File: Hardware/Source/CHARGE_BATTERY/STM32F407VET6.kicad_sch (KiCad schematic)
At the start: 3 parts, among them U2 STM32F407VET6, Y1 Crystal_8MHz_SMD-4PIN

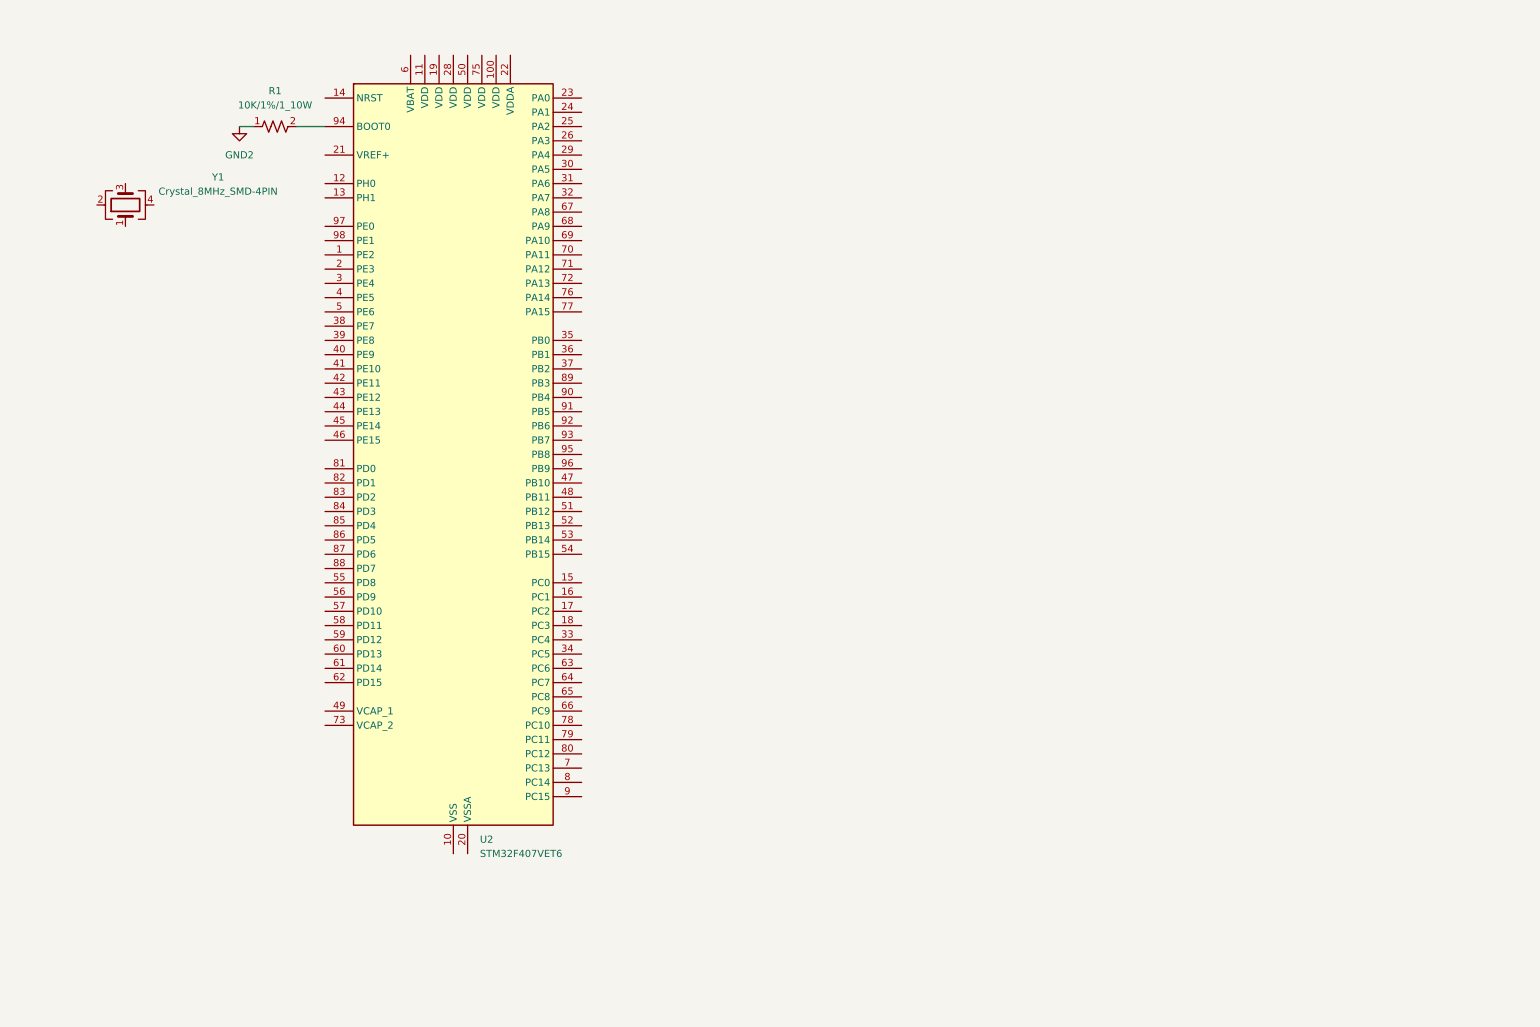
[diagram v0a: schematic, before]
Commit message: Combine Sche in Source: PFC, LLC, F1, F4, ESP32
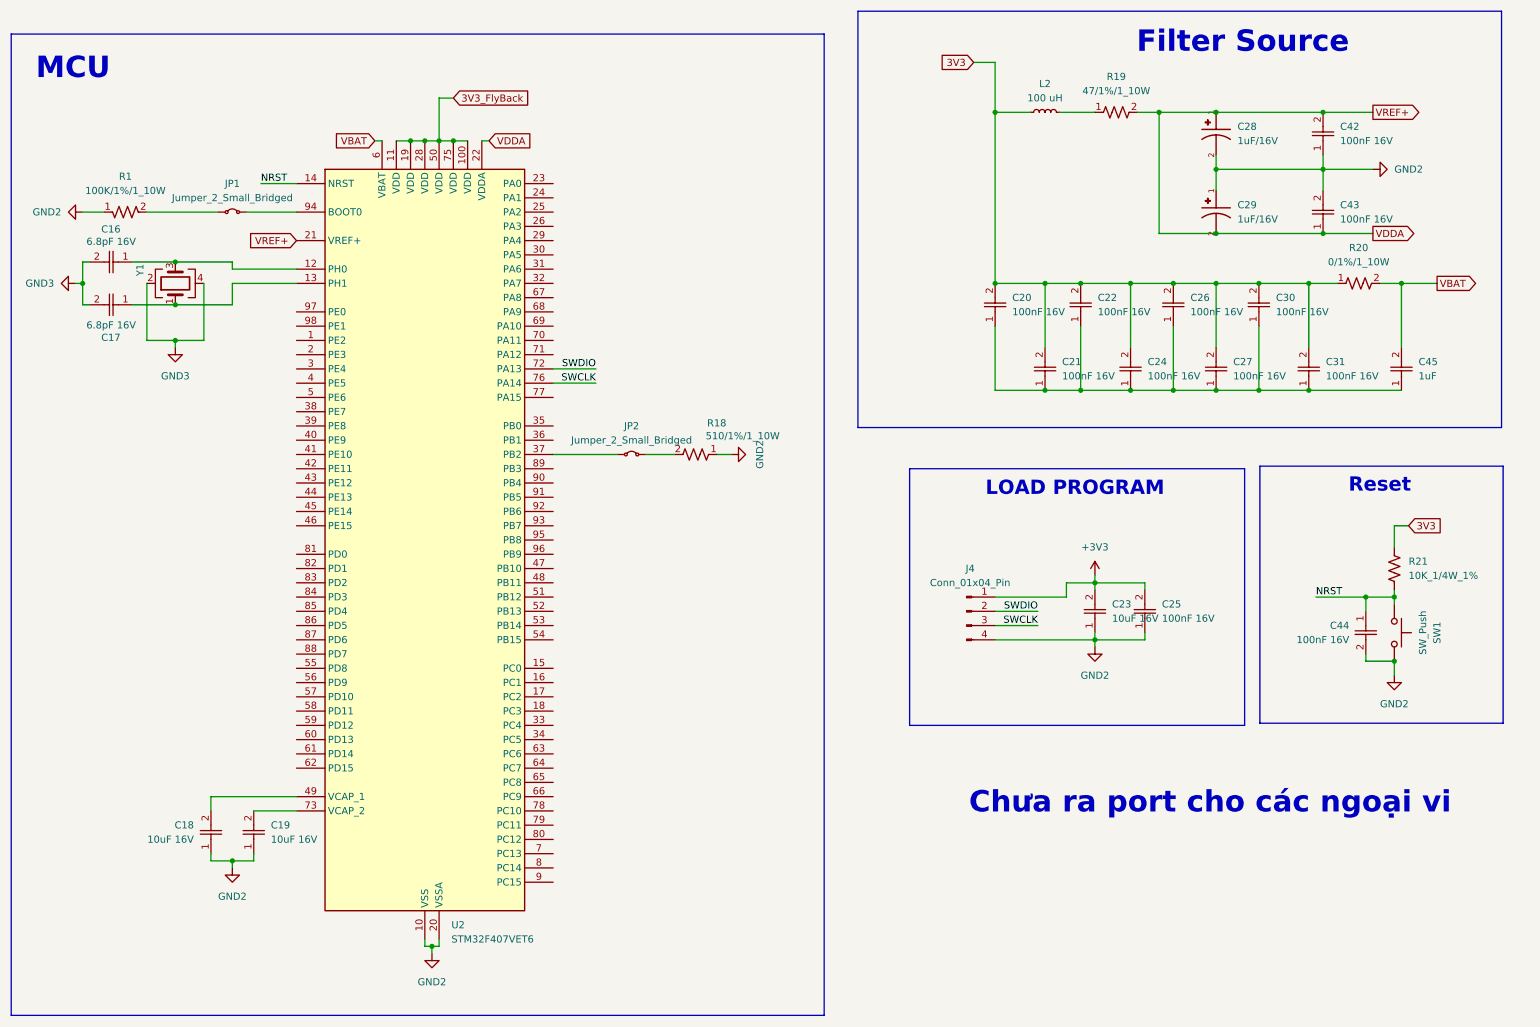
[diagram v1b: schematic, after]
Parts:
- removed R1: 10K/1%/1_10W, charge_battery_footprint_lib:Res_10K_0603, symbol charge_battery_sym_lib:Res_10K_0603_1%
- added C16, C17: 6.8pF 16V, charge_battery_footprint_lib:C_0603_1608Metric, symbol charge_battery_sym_lib:Ceramic_Cap_SMD_100nF_16V
- added C18, C19, C23: 10uF 16V, charge_battery_footprint_lib:Ceramic_Cap_10uF_16V, symbol charge_battery_sym_lib:Ceramic_Cap_SMD_10uF_16V
- added C20, C21, C22, C24, C25, C26, C27, C30, C31, C42, C43, C44: 100nF 16V, charge_battery_footprint_lib:C_0603_1608Metric, symbol charge_battery_sym_lib:Ceramic_Cap_SMD_100nF_16V
- added C28, C29: 1uF/16V, charge_battery_footprint_lib:Cap_Tantalum_1uF_16V, symbol charge_battery_sym_lib:Cap_Tantalum_1uF_16V
- added C45: 1uF, charge_battery_footprint_lib:Ceramic_Cap_Hole_1uF_50V, symbol charge_battery_sym_lib:Ceramic_Cap_Hole_1uF_50V_
- added J4: Conn_01x04_Pin, symbol Connector:Conn_01x04_Pin
- added JP1, JP2: Jumper_2_Small_Bridged, TestPoint:TestPoint_2Pads_Pitch2.54mm_Drill0.8mm, symbol Jumper:Jumper_2_Small_Bridged
- added L2: 100 uH, symbol Device:L_Small
- added R1: 100K/1%/1_10W, charge_battery_footprint_lib:Res_200K_0603, symbol charge_battery_sym_lib:Res_200K_0603_1%
- added R18: 510/1%/1_10W, charge_battery_footprint_lib:Res_10K_0603, symbol charge_battery_sym_lib:Res_10K_0603_1%
- added R19: 47/1%/1_10W, charge_battery_footprint_lib:Res_10K_0603, symbol charge_battery_sym_lib:Res_10K_0603_1%
- added R20: 0/1%/1_10W, charge_battery_footprint_lib:Res_10K_0603, symbol charge_battery_sym_lib:Res_10K_0603_1%
- added R21: 10K_1/4W_1%, charge_battery_footprint_lib:Res_10K_1_4W_1%, symbol charge_battery_sym_lib:Res_hole_10K_1/4W_1%
- added SW1: SW_Push, charge_battery_footprint_lib:SW_SMD, symbol charge_battery_sym_lib:SW_Push
- Y1: footprint charge_battery_footprint_lib:Crystal_8MHz_SMD-4PIN -> charge_battery_footprint_lib:IPP65R095C7
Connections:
- net GND2: now also U2.10 (VSS), U2.20 (VSSA), U2.27 (VSS), U2.74 (VSS), U2.99 (VSS), C18.1, C19.1, C23.1, C25.1, C28.2, C29.1, C42.1, C43.2, C44.2, J4.4 (Pin_4), R1.1, R18.1, SW1.1
- net at Y1.1: now also U2.13 (PH1), C17.1
- net GND3: now reaches Y1.2
- net GND3: now also Y1.4, C16.2, C17.2
- net at Y1.3: now also U2.12 (PH0), C16.1
- net at U2.94 (BOOT0): now also JP1.2 (B)
- net 3V3_FlyBack: now reaches U2.100 (VDD)
- net 3V3_FlyBack: now also U2.11 (VDD), U2.19 (VDD), U2.28 (VDD), U2.50 (VDD), U2.75 (VDD)
- net NRST: now reaches U2.14 (NRST)
- net NRST: now also C44.1, R21.1, SW1.2
- net VDDA: now reaches U2.21 (VREF+)
- net VDDA: now also U2.22 (VDDA), C28.1, C29.2, C42.2, C43.1, R19.2
- net at U2.37 (PB2): now also JP2.1 (A)
- net at U2.49 (VCAP_1): now also C18.2
- net VBAT: now reaches U2.6 (VBAT)
- net VBAT: now also C45.2, R20.2
- net SWDIO: now reaches U2.72 (PA13)
- net SWDIO: now also J4.2 (Pin_2)
- net at U2.73 (VCAP_2): now also C19.2
- net SWCLK: now reaches U2.76 (PA14)
- net SWCLK: now also J4.3 (Pin_3)
- new net: C20.1, C21.1, C22.1, C24.1, C26.1, C27.1, C30.1, C31.1, C45.1
- new net: JP1.1 (A), R1.2
- new net: L2.2, R19.1
- new net: JP2.2 (B), R18.2
- new net +3V3: C23.2, C25.2, J4.1 (Pin_1)
- new net 3V3: C20.2, C21.2, C22.2, C24.2, C26.2, C27.2, C30.2, C31.2, L2.1, R20.1, R21.2
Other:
- note added: "Chưa ra port cho các ngoại vi"
- note added: "Filter Source"
- note added: "LOAD PROGRAM"
- note added: "MCU"
- note added: "Reset"

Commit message: Merge branch 'dev_hardware' of https://github.com/DONGKHOA/CHARGE_BATTERY into dev_hardware
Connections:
- net 3V3 is gone; now on net +3V3: C20.2, C21.2, C22.2, C24.2, C26.2, C27.2, C30.2, C31.2, L2.1, R20.1, R21.2
- net 3V3_FlyBack is gone; now on net +3V3: U2.100 (VDD), U2.11 (VDD), U2.19 (VDD), U2.28 (VDD), U2.50 (VDD), U2.75 (VDD)
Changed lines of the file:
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@@
-	(wire
-		(pts
-			(xy 186.69 24.13) (xy 190.5 24.13)
-		)
-		(stroke
-			(width 0)
-			(type default)
-		)
-	)
 	(wire
 		(pts
@@
 	(wire
 		(pts
-			(xy 93.98 30.48) (xy 91.44 30.48)
-		)
-		(stroke
-			(width 0)
-			(type default)
-		)
-	)
-	(wire
-		(pts
 			(xy 59.69 45.72) (xy 66.04 45.72)
 		)
@@
 	(wire
 		(pts
-			(xy 264.16 106.68) (xy 261.62 106.68)
-		)
-		(stroke
-			(width 0)
-			(type default)
-		)
-	)
-	(wire
-		(pts
 			(xy 58.42 157.48) (xy 66.04 157.48)
 		)
@@
 	(wire
 		(pts
-			(xy 190.5 24.13) (xy 190.5 33.02)
+			(xy 190.5 26.67) (xy 190.5 33.02)
 		)
 		(stroke
@@
 	(wire
 		(pts
-			(xy 261.62 106.68) (xy 261.62 110.49)
+			(xy 261.62 107.95) (xy 261.62 110.49)
 		)
 		(stroke
@@
 		)
 	)
-	(global_label "3V3"
-		(shape input)
-		(at 186.69 24.13 180)
+	(global_label "VREF+"
+		(shape output)
+		(at 257.81 33.02 0)
 		(fields_autoplaced yes)
 		(effects
@@
 				(size 1.27 1.27)
 			)
-			(justify right)
-		)
-		(property "Intersheetrefs" "${INTERSHEET_REFS}"
-			(at 180.1972 24.13 0)
-			(effects
-				(font
-					(size 1.27 1.27)
-				)
-				(justify right)
-				(hide yes)
-			)
-		)
-	)
-	(global_label "VREF+"
-		(shape output)
-		(at 257.81 33.02 0)
-		(fields_autoplaced yes)
-		(effects
-			(font
-				(size 1.27 1.27)
-			)
 			(justify left)
 		)
 		(property "Intersheetrefs" "${INTERSHEET_REFS}"
 			(at 266.9638 33.02 0)
-			(effects
-				(font
-					(size 1.27 1.27)
-				)
-				(justify left)
-				(hide yes)
-			)
-		)
-	)
-	(global_label "3V3"
-		(shape input)
-		(at 264.16 106.68 0)
-		(fields_autoplaced yes)
-		(effects
-			(font
-				(size 1.27 1.27)
-			)
-			(justify left)
-		)
-		(property "Intersheetrefs" "${INTERSHEET_REFS}"
-			(at 270.6528 106.68 0)
-			(effects
-				(font
-					(size 1.27 1.27)
-				)
-				(justify left)
-				(hide yes)
-			)
-		)
-	)
-	(global_label "3V3_FlyBack"
-		(shape input)
-		(at 93.98 30.48 0)
-		(fields_autoplaced yes)
-		(effects
-			(font
-				(size 1.27 1.27)
-			)
-			(justify left)
-		)
-		(property "Intersheetrefs" "${INTERSHEET_REFS}"
-			(at 108.6975 30.48 0)
 			(effects
 				(font
@@
 	)
 	(symbol
+		(lib_id "power:+3V3")
+		(at 190.5 26.67 0)
+		(unit 1)
+		(exclude_from_sim no)
+		(in_bom yes)
+		(on_board yes)
+		(dnp no)
+		(fields_autoplaced yes)
+		(property "Reference" "#PWR058"
+			(at 190.5 30.48 0)
+			(effects
+				(font
+					(size 1.27 1.27)
+				)
+				(hide yes)
+			)
+		)
+		(property "Value" "+3V3"
+			(at 190.5 21.59 0)
+			(effects
+				(font
+					(size 1.27 1.27)
+				)
+			)
+		)
+		(property "Footprint" ""
+			(at 190.5 26.67 0)
+			(effects
+				(font
+					(size 1.27 1.27)
+				)
+				(hide yes)
+			)
+		)
+		(property "Datasheet" ""
+			(at 190.5 26.67 0)
+			(effects
+				(font
+					(size 1.27 1.27)
+				)
+				(hide yes)
+			)
+		)
+		(property "Description" "Power symbol creates a global label with name \"+3V3\""
+			(at 190.5 26.67 0)
+			(effects
+				(font
+					(size 1.27 1.27)
+				)
+				(hide yes)
+			)
+		)
+		(pin "1"
+		)
+		(instances
+			(project "CHARGE_BATTERY"
+				(path "/52eaef32-c16d-4834-ac94-ac67b58aa1d2/e14e8644-1ffb-4f6b-8c96-343794878f82"
+					(reference "#PWR058")
+					(unit 1)
+				)
+			)
+		)
+	)
+	(symbol
 		(lib_id "charge_battery_sym_lib:Ceramic_Cap_SMD_100nF_16V")
 		(at 220.218 67.31 90)
@@
 	)
 	(symbol
+		(lib_id "power:+3V3")
+		(at 91.44 30.48 0)
+		(unit 1)
+		(exclude_from_sim no)
+		(in_bom yes)
+		(on_board yes)
+		(dnp no)
+		(fields_autoplaced yes)
+		(property "Reference" "#PWR056"
+			(at 91.44 34.29 0)
+			(effects
+				(font
+					(size 1.27 1.27)
+				)
+				(hide yes)
+			)
+		)
+		(property "Value" "+3V3"
+			(at 91.44 25.4 0)
+			(effects
+				(font
+					(size 1.27 1.27)
+				)
+			)
+		)
+		(property "Footprint" ""
+			(at 91.44 30.48 0)
+			(effects
+				(font
+					(size 1.27 1.27)
+				)
+				(hide yes)
+			)
+		)
+		(property "Datasheet" ""
+			(at 91.44 30.48 0)
+			(effects
+				(font
+					(size 1.27 1.27)
+				)
+				(hide yes)
+			)
+		)
+		(property "Description" "Power symbol creates a global label with name \"+3V3\""
+			(at 91.44 30.48 0)
+			(effects
+				(font
+					(size 1.27 1.27)
+				)
+				(hide yes)
+			)
+		)
+		(pin "1"
+		)
+		(instances
+			(project ""
+				(path "/52eaef32-c16d-4834-ac94-ac67b58aa1d2/e14e8644-1ffb-4f6b-8c96-343794878f82"
+					(reference "#PWR056")
+					(unit 1)
+				)
+			)
+		)
+	)
+	(symbol
 		(lib_id "charge_battery_sym_lib:Res_10K_0603_1%")
 		(at 209.804 39.37 0)
@@
 					(unit 1)
 				)
+			)
+		)
+	)
+	(symbol
+		(lib_id "power:+3V3")
+		(at 261.62 107.95 0)
+		(unit 1)
+		(exclude_from_sim no)
+		(in_bom yes)
+		(on_board yes)
+		(dnp no)
+		(fields_autoplaced yes)
+		(property "Reference" "#PWR057"
+			(at 261.62 111.76 0)
+			(effects
+				(font
+					(size 1.27 1.27)
+				)
+				(hide yes)
+			)
+		)
+		(property "Value" "+3V3"
+			(at 261.62 102.87 0)
+			(effects
+				(font
+					(size 1.27 1.27)
+				)
+			)
+		)
+		(property "Footprint" ""
+			(at 261.62 107.95 0)
+			(effects
+				(font
+					(size 1.27 1.27)
+				)
+				(hide yes)
+			)
+		)
+		(property "Datasheet" ""
+			(at 261.62 107.95 0)
+			(effects
+				(font
+					(size 1.27 1.27)
+				)
+				(hide yes)
+			)
+		)
+		(property "Description" "Power symbol creates a global label with name \"+3V3\""
+			(at 261.62 107.95 0)
+			(effects
+				(font
+					(size 1.27 1.27)
+				)
+				(hide yes)
+			)
+		)
+		(pin "1"
+		)
+		(instances
+			(project "CHARGE_BATTERY"
+				(path "/52eaef32-c16d-4834-ac94-ac67b58aa1d2/e14e8644-1ffb-4f6b-8c96-343794878f82"
+					(reference "#PWR057")
+					(unit 1)
+				)
